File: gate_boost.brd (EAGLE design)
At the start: 74.9 x 45.3 mm, 57 parts, among them IC1 LM324D, IC2 SP34063A_BOOST_REG

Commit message: prior change to charge pump
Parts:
- C1: value (none) -> 1500pf
- R19: value (none) -> 68k
- R20: value (none) -> 180
- R21: value (none) -> 0.22
- R23: value (none) -> 3k3
- R24: value (none) -> 6k2

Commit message: charge pump
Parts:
- removed D10, D9: CGRM4001-G, diode:SOD-123_MINI-SMA
- removed D5, D6, D7, D8: PD3S160, diode:POWERDI323
- removed JP1: (no value), pinhead:1X03
- removed L1: (no value), wuerth-elektronik:WE-PD_S/M
- removed LED5: (no value), adafruit:LED3MM
- removed PWR1, PWR2: 2.1MMJACKTHM, adafruit:PJ-102A
- removed R22: (no value), rcl:R0805
- removed R23: 3k3, rcl:R0805
- removed R24: 6k2, rcl:R0805
- added C10, C11, C12, C5: (no value), resistor:C0805
- added C6: (no value), rcl:SMC_A
- added C7, C8: 10u, rcl:SMC_A
- added C9: (no value), rcl:E2-5
- added CLK_LED2: (no value), led:LED3MM
- added IC3: LM27675M5_CHARGEPUMP, jason_eagle6:SOT23-6
- added IC4: LM358D, linear:SO08
- added S1: (no value), switch-dil:DIP02YL
- added U$1, U$2: PWR_SOCKET_2_1MM, jason_eagle6:PWR_SOCKET_2_1MM
- C1: value 1500pf -> (none); device rcl:C0805 -> resistor:C0805
- C2: device rcl:C0805 -> resistor:C0805
- C3, C4: device rcl:E2,5-6 -> resistor:C0805
- D1, D2, D3, D4: value PD3S160 -> MBR0520LT; device diode:POWERDI323 -> diode:SOD123
- IC1: value LM324D -> LM358D; device linear:SO14 -> linear:SO08
- IC2: value SP34063A_BOOST_REG -> REG1117; device jason_eagle6:SOIC8 -> burr-brown:SOT223
- IN1, IN2, IN3, IN4, OUT1, OUT2, OUT3, OUT4: value TRUCONNECTJACK -> VERTICAL_3_5MM_SOCKET; device jason_eagle6:TRUCONNECTJACK -> jason_eagle6:VERTICAL_3_5MM_SOCKET
- LED1, LED2, LED3, LED4: device adafruit:LED3MM -> led:LED3MM
- R1, R10, R13, R2: value (none) -> 1K
- R12, R16, R17, R18, R6, R9: value (none) -> 100k
- R19: value 68k -> (none)
- R20: value 180 -> (none)
- R21: value 0.22 -> 1K
- moved D2 67.1 mm to (72.4, 27.9), turned to 90 degrees
- moved D3 62.7 mm to (74.9, 27.9)
- moved D4 60.6 mm to (77.5, 27.9), turned to 90 degrees
- moved D1 55.1 mm to (57.1, 34.3), turned to 180 degrees
- moved R5 51.8 mm to (6.35, 15.2), turned to 0 degrees
- moved R3 47.4 mm to (31.8, 15.2), turned to 0 degrees
- moved R4 46.0 mm to (19.1, 15.2), turned to 0 degrees
- moved C2 45.0 mm to (52.1, 15.2), turned to 0 degrees
- moved R8 44.9 mm to (16.5, 30.5)
- moved C4 44.9 mm to (26.7, 15.2), turned to 0 degrees
- moved R1 40.6 mm to (44.5, 48.3), turned to 0 degrees
- moved R7 38.6 mm to (19.8, 30.5), turned to 90 degrees
- moved IC2 36.9 mm to (61.0, 19.1), turned to 180 degrees
- moved R6 33.5 mm to (22.9, 30.5)
- moved C1 33.3 mm to (39.4, 15.2), turned to 0 degrees
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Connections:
- removed net N$18: IC1.8, LED3.A, R14.1
- removed net N$22: IC2.8, R20.1
- removed net N$24: C4.+, D10.C, IC2.6, R21.1
- removed net N$25: D10.A, PWR1.RING, PWR2.RING
- removed net N$27: LED1.K, R9.2
- removed net N$30: LED2.K, R11.2
- removed net N$31: LED3.K, R13.2
- removed net N$32: LED4.K, R15.2
- removed net N$34: LED5.K, R22.2
- removed net N$6: D5.C, D6.A, IC1.10, R5.2, R6.2
- removed net V+: C2.2, C3.+, D2.C, D4.C, D6.C, D8.C, D9.C, IC1.4, LED5.A, R18.2, R19.1
- new net +10V: C6.+, D1.C, D3.A, D4.A, IC3.5
- new net +5V: C12.1, C7.+, CLK_LED2.A, D1.A, IC2.2, IC3.1, R16.2, R6.2
- new net IN1: IN1.4, LED1.A, R12.2
- new net IN2: IN2.4, LED2.A, R9.2
- new net IN3: IN3.4, LED3.A, R17.2
- new net IN4: IN4.4, LED4.A, R18.2
- new net N$38: C8.+, IC3.6
- new net N$39: C8.-, IC3.3
- new net VGATE1: C10.1, D3.C, IC4.8, S1.1
- new net VGATE2: C3.1, D4.C, IC1.8, S1.2
- new net VIN: C11.1, C9.+, D2.C, IC2.3, S1.3, S1.4
- net GND: now also C10.2, C11.2, C12.2, C2.2, C3.2, C4.2, C5.2, C6.-, C7.-, C9.-, IC1.4, IC2.1, IC3.2, IC3.4, IC4.4, IN1.2, IN2.2, IN3.2, IN4.2, OUT1.2, OUT2.2, OUT3.2, OUT4.2, R1.2, R10.2, R13.2, R2.2, R21.2, U$1.PIN, U$2.PIN; no longer C2.1, C3.-, C4.-, D1.A, D3.A, D5.A, D7.A, IC1.11, IC2.2, IC2.4, IN1.SLEEVE, IN2.SLEEVE, IN3.SLEEVE, IN4.SLEEVE, OUT1.SLEEVE, OUT2.SLEEVE, OUT3.SLEEVE, OUT4.SLEEVE, PWR1.TIP, PWR2.TIP, R1.1, R11.1, R13.1, R17.1, R22.1, R24.1, R3.1, R5.1, R9.1
- net N$1: now also IC4.2, IC4.6, R6.1, R7.2; no longer IN1.TIP, IN1.TIP_NC, R2.1
- net N$10: now also IC1.7, R14.1, R19.1; no longer IC1.13, IC1.2, IC1.6, IC1.9, R17.2, R18.1
- net N$11: now also IC1.1, R20.1, R3.1; no longer OUT1.TIP, OUT1.TIP_NC, R10.2
- net N$12: now also IC4.7, R4.1, R8.1; no longer OUT2.TIP, OUT2.TIP_NC, R12.2
- net N$13: now also IC1.2, IC1.6, R15.2, R16.1; no longer OUT3.TIP, OUT3.TIP_NC, R14.2
- net N$14: now also LED3.K, R2.1; no longer OUT4.TIP, OUT4.TIP_NC, R16.2
- net N$15: now also LED4.K, R1.1; no longer C1.1, IC2.3
- net N$16: now also IC1.3, R17.1, R20.2; no longer D9.A, IC2.1, L1.2
- net N$17: now also IC1.5, R18.1, R19.2; no longer IC1.7, LED2.A, R12.1
- net N$19: now also C5.1, OUT1.4, R5.2; no longer IC1.14, LED4.A, R16.1
- net N$2: now also LED1.K, R13.1; no longer IN2.TIP, IN2.TIP_NC, R4.1
- net N$20: now also C4.1, OUT2.4, R4.2; no longer IC2.5, JP1.2, R19.2, R23.1
- net N$21: now also D2.A, U$1.BARREL, U$2.BARREL; no longer JP1.1, R23.2, R24.2
- net N$23: now also CLK_LED2.K, R21.1; no longer IC2.7, L1.1, R20.2, R21.2
- net N$3: now also LED2.K, R10.1; no longer IN3.TIP, IN3.TIP_NC, R6.1
- net N$4: now also IC4.3, R11.2, R12.1; no longer IN4.TIP, IN4.TIP_NC, R8.1
- net N$5: now also IC4.5, R9.1; no longer D7.C, D8.A, IC1.12, R7.2
- net N$7: now also C1.1, OUT3.4; no longer D3.C, D4.A, IC1.5, R4.2
- net N$8: now also C2.1, OUT4.4, R14.2; no longer D1.C, D2.A, IC1.3, R1.2, R2.2
- net N$9: now also IC4.1, R11.1, R5.1; no longer IC1.1, LED1.A, R10.1
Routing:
- net V+: track 134.7 -> 0.00 mm, vias 5 -> 0
- net VGATE1: track 0.00 -> 95.6 mm, vias 0 -> 1
- net +5V: track 0.00 -> 91.8 mm, vias 0 -> 4
- net VGATE2: track 0.00 -> 72.7 mm, vias 0 -> 1
- net N$25: track 53.9 -> 0.00 mm
- net GND: track 49.0 -> 0.00 mm, vias 13 -> 0
- net N$19: track 49.2 -> 8.42 mm, vias 1 -> 0
- net +10V: track 0.00 -> 32.0 mm, vias 0 -> 2
- net N$21: track 9.02 -> 38.3 mm
- net VIN: track 0.00 -> 27.6 mm, vias 0 -> 1
- net N$20: track 34.3 -> 8.42 mm, vias 2 -> 0
- net N$18: track 25.6 -> 0.00 mm, vias 1 -> 0
- net N$6: track 25.4 -> 0.00 mm, vias 2 -> 0
- net N$7: track 33.8 -> 8.42 mm, vias 2 -> 0
- net N$24: track 22.2 -> 0.00 mm
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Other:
- board size 74.9 x 45.3 mm -> 87.6 x 38.1 mm
- board text removed: "PWR1"
- board text removed: "PWR2"
- board text removed: "QUAD GATE BOOST rev 1"
- board text removed: "hotchk155"

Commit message: getting there
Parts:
- C10, C11: value (none) -> 10u; device resistor:C0805 -> rcl:SMC_A
- C12: device resistor:C0805 -> rcl:E2-5
- C6: device rcl:SMC_A -> resistor:C0805
- C7, C8: value 10u -> (none); device rcl:SMC_A -> resistor:C0805
- C9: device rcl:E2-5 -> rcl:SMC_A
- IC2: value REG1117 -> LM358D; device burr-brown:SOT223 -> linear:SO08
- IC4: value LM358D -> REG1117; device linear:SO08 -> burr-brown:SOT223
- R10, R13, R21: value 1K -> (none)
- R17: value 100k -> 1K
- R18, R9: value 100k -> (none)
- R2: value 1K -> 100k
- R3, R5, R7: value (none) -> 1K
- R4, R8: value (none) -> 100k
- moved R18 56.4 mm to (6.35, 15.2), turned to 0 degrees
- moved IC4 52.1 mm to (61.0, 19.1), turned to 180 degrees
- moved C10 47.6 mm to (57.1, 26.7), turned to 0 degrees
- moved R5 41.7 mm to (31.8, 48.3)
- moved R8 39.8 mm to (52.1, 48.3), turned to 180 degrees
- moved R1 38.1 mm to (6.35, 48.3)
- moved R3 35.4 mm to (19.1, 48.3)
- moved C1 34.9 mm to (10.2, 34.3), turned to 180 degrees
- moved R4 33.9 mm to (26.7, 48.3), turned to 180 degrees
- moved R17 32.5 mm to (67.3, 31.8)
- moved R7 30.4 mm to (44.5, 48.3), turned to 0 degrees
- moved R13 29.0 mm to (29.2, 30.5), turned to 270 degrees
- moved R9 29.0 mm to (3.81, 30.5), turned to 270 degrees
- moved C3 28.8 mm to (14.0, 15.2), turned to 0 degrees
- moved R21 28.2 mm to (44.5, 15.2), turned to 0 degrees
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- renumbered CLK_LED2 to PWR, LED1 to A, LED2 to B, LED3 to C, LED4 to D, S1 to SW1
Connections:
- net +10V: now also C9.+; no longer C6.+
- net +5V: now also C10.+, C8.1, IC4.2, R12.2; no longer C12.1, C7.+, IC2.2, R6.2
- net GND: now also C10.-, C12.-, C6.2, C7.2, C8.2, IC2.4, IC4.1, R11.1, R17.2, R3.2, R5.2, R7.2; no longer C10.2, C11.2, C12.2, C6.-, C7.-, IC2.1, IC4.4, R10.2, R13.2, R2.2, R21.2, R7.1
- net IN1: now also R2.2; no longer R12.2
- net IN2: now also R4.2; no longer R9.2
- net IN3: now also R6.2; no longer R17.2
- net IN4: now also R8.2; no longer R18.2
- net N$1: now also IC1.2, IC1.6, R11.2, R12.1; no longer IC4.2, IC4.6, R6.1, R7.2
- net N$10: now also IC2.7, R21.1; no longer IC1.7, R19.1
- net N$11: now also IC2.1, R13.1; no longer IC1.1, R3.1
- net N$12: now also IC1.7, R10.1, R19.1; no longer IC4.7, R4.1, R8.1
- net N$13: now also IC2.2, IC2.6; no longer IC1.2, IC1.6
- net N$14: now also R5.1; no longer R2.1
- net N$15: now also R7.1; no longer R1.1
- net N$16: now also IC2.3, R13.2, R6.1; no longer IC1.3, R17.1, R20.2
- net N$17: now also IC2.5, R14.2, R8.1; no longer IC1.5, R18.1, R19.2
- net N$19: now also C3.1, R18.2; no longer C5.1, R5.2
- net N$2: now also R1.1; no longer R13.1
- net N$20: now also R19.2; no longer R4.2
- net N$23: now also R17.1; no longer R21.1
- net N$3: now also R3.1; no longer R10.1
- net N$38: now also C11.+; no longer C8.+
- net N$39: now also C11.-; no longer C8.-
- net N$4: now also IC1.3, R2.1, R9.2; no longer IC4.3, R11.2, R12.1
- net N$5: now also IC1.5, R10.2, R4.1; no longer IC4.5, R8.2, R9.1
- net N$7: now also C5.1, R20.2; no longer C1.1, R3.2
- net N$8: now also C6.1, R21.2; no longer C2.1, R14.2
- net N$9: now also IC1.1, R18.1, R9.1; no longer IC4.1, R11.1, R5.1
- net VGATE1: now also C1.1, IC1.8; no longer C10.1, IC4.8
- net VGATE2: now also C2.1, IC2.8; no longer C3.1, IC1.8
- net VIN: now also C12.+, C7.1, IC4.3; no longer C11.1, C9.+, IC2.3
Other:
- board text added: "CV.OCD Gate Boost v1"
- board text added: "six4pix.com/cvocd"

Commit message: component values
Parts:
- R13, R14: value (none) -> 2m2
- R15: value (none) -> 47k
- R16: value 100k -> 47k
- R20, R21: value (none) -> 1k

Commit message: aye
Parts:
- R10, R9: value (none) -> 2m2
- R11: value (none) -> 47k
- R12: value 100k -> 47k
- R18, R19: value (none) -> 1k

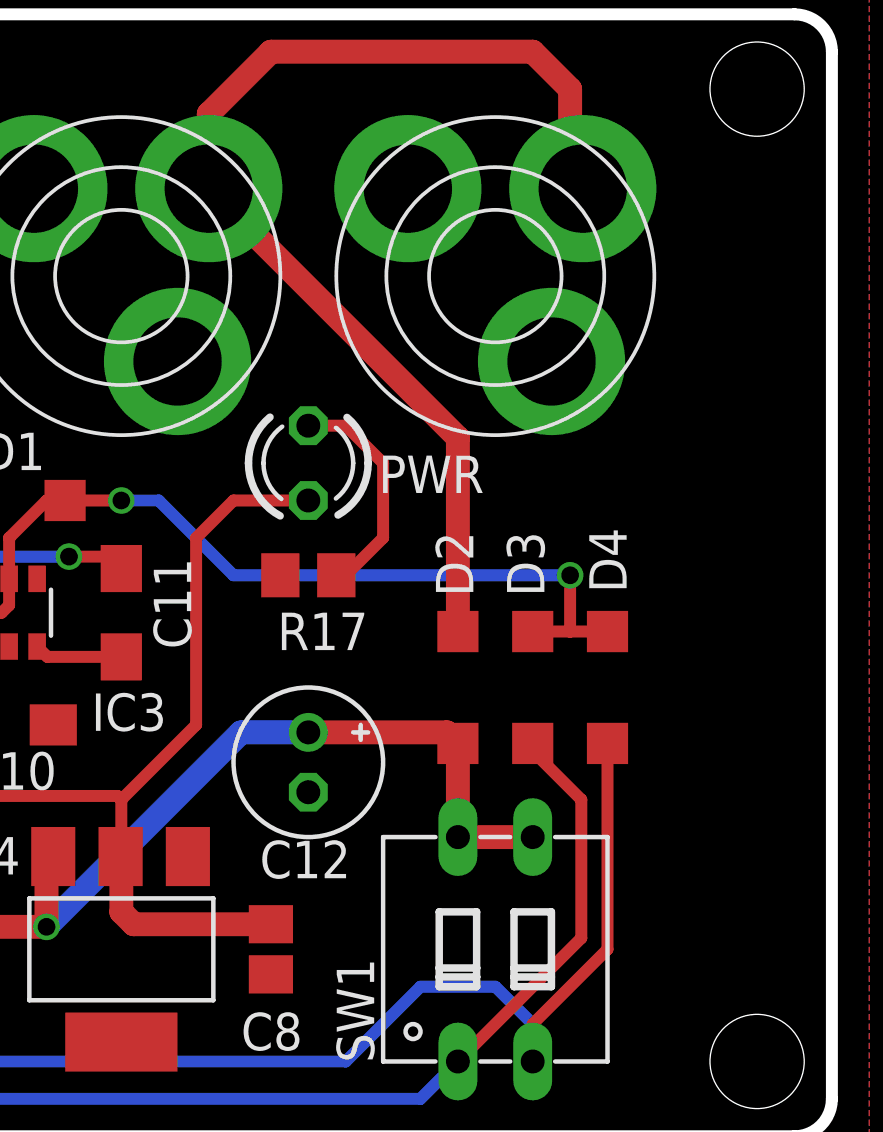
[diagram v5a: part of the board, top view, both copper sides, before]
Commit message: V2 additional schottky on VIN
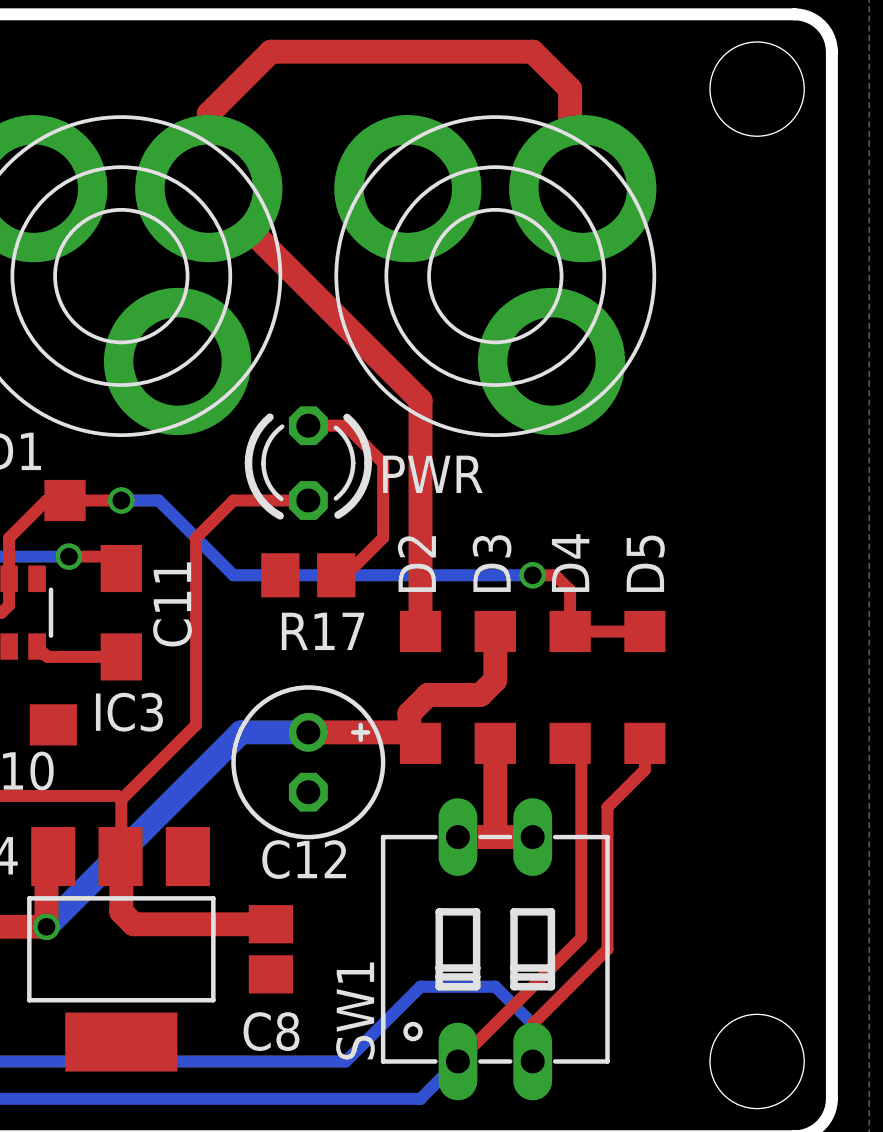
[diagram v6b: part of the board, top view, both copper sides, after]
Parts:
- added D5: MBR0520LT, diode:SOD123
- moved D3 1.27 mm to (73.7, 27.9)
- moved D2 1.27 mm to (71.1, 27.9)
- moved D4 1.27 mm to (76.2, 27.9)
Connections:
- new net N$6: D3.C, SW1.3, SW1.4
- net +10V: now also D5.A; no longer D3.A
- net VGATE1: now also D4.C; no longer D3.C
- net VGATE2: now also D5.C; no longer D4.C
- net VIN: now also D3.A; no longer SW1.3, SW1.4
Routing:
- net N$6: track 0.00 -> 5.72 mm
- net VIN: track 27.6 -> 26.3 mm
- net VGATE2: track 72.7 -> 73.2 mm
- net VGATE1: track 95.6 -> 95.0 mm
- net N$21: track 38.3 -> 37.8 mm
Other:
- board text added: "CV.OCD Gate Boost v2"
- board text removed: "CV.OCD Gate Boost v1"
